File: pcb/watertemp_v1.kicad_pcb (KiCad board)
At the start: 2 copper layers, 43 x 90 mm, 31 parts, among them J1 RN2483 Ext, J2 SWD, J3 I2C, J4 UART1, J5 UART2, U1 LPC11U24FBD48, U2 RN2483, U3 SHT21, U4 LP5907-Q1, U5 DS18B20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

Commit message: Finish routing first version
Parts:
- added C6: 100nF, Capacitors_SMD:C_0805, F.Cu at (68.8, 53.8)
- added C7: 100nF, Capacitors_SMD:C_0805, F.Cu at (63.6, 65.8)
- added REF**: VIA-0.6mm, StitchingVia:VIA-0.6mm, F.Cu at (73.0, 63.9)
- added REF**: VIA-0.6mm, StitchingVia:VIA-0.6mm, F.Cu at (61.3, 106.7)
- added REF**: VIA-0.6mm, StitchingVia:VIA-0.6mm, F.Cu at (62.1, 105.9)
- added REF**: VIA-0.6mm, StitchingVia:VIA-0.6mm, F.Cu at (60.5, 104.4)
- added REF**: VIA-0.6mm, StitchingVia:VIA-0.6mm, F.Cu at (59.7, 105.2)
- added REF**: VIA-0.6mm, StitchingVia:VIA-0.6mm, F.Cu at (58.9, 105.9)
- added REF**: VIA-0.6mm, StitchingVia:VIA-0.6mm, F.Cu at (72.3, 51.7)
- added REF**: VIA-0.6mm, StitchingVia:VIA-0.6mm, F.Cu at (67.7, 63.9)
- added REF**: VIA-0.6mm, StitchingVia:VIA-0.6mm, F.Cu at (75.6, 56.5)
- added REF**: VIA-0.6mm, StitchingVia:VIA-0.6mm, F.Cu at (65.3, 102.5)
- added REF**: VIA-0.6mm, StitchingVia:VIA-0.6mm, F.Cu at (64.5, 103.3)
- added REF**: VIA-0.6mm, StitchingVia:VIA-0.6mm, F.Cu at (67.3, 103.6)
- added REF**: VIA-0.6mm, StitchingVia:VIA-0.6mm, F.Cu at (66.5, 104.4)
- added REF**: VIA-0.6mm, StitchingVia:VIA-0.6mm, F.Cu at (65.8, 105.2)
- added REF**: VIA-0.6mm, StitchingVia:VIA-0.6mm, F.Cu at (60.6, 107.4)
- R1, R2, R3, R4, R5, R6, R7: footprint Resistors_SMD:R_0805_HandSoldering -> Resistors_SMD:R_0805
- moved R7 94.6 mm to (30.4, 74.0)
- moved D3 92.1 mm to (32.0, 65.0)
- moved R2 84.1 mm to (36.3, 61.2), turned to 180 degrees
- moved R3 82.6 mm to (36.3, 65.0), turned to 180 degrees
- moved R6 82.1 mm to (30.4, 76.6)
- moved D1 80.4 mm to (32.0, 57.4)
- moved R8 77.8 mm to (30.5, 99.5), turned to 270 degrees
- moved U5 77.0 mm to (34.2, 103.4), turned to 180 degrees
- moved R1 73.8 mm to (36.3, 57.4), turned to 180 degrees
- moved D2 73.6 mm to (32.0, 61.2)
- moved J3 43.4 mm to (34.2, 71.5), turned to 0 degrees
- moved J1 40.0 mm to (75.9, 71.9)
- moved R4 38.2 mm to (63.6, 56.8), turned to 270 degrees
- moved R5 24.5 mm to (75.0, 68.8)
- moved J2 21.3 mm to (74.0, 47.0), turned to 0 degrees
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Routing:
- net 3.3V: track 3.92 -> 236.2 mm, vias 0 -> 2
- net SCL: track 0.00 -> 120.4 mm, vias 0 -> 2
- net SDA: track 0.00 -> 114.0 mm, vias 0 -> 2
- net UC-TX0: track 0.00 -> 83.3 mm, vias 0 -> 2
- net UC-RX0: track 0.00 -> 80.0 mm, vias 0 -> 2
- net DS18B20: track 0.00 -> 62.9 mm, vias 0 -> 2
- net LED1: track 0.00 -> 45.6 mm, vias 0 -> 2
- net LED2: track 0.00 -> 35.8 mm, vias 0 -> 2
- net LED3: track 0.00 -> 35.2 mm, vias 0 -> 2
- net UC-TX1: track 0.00 -> 32.2 mm, vias 0 -> 1
- net UC-RX1: track 0.00 -> 31.8 mm, vias 0 -> 1
- net PGD_INT: track 0.00 -> 30.2 mm, vias 0 -> 1
- net PGC_INT: track 0.00 -> 29.9 mm, vias 0 -> 1
- net RN_RST: track 0.00 -> 27.5 mm
- net NRESET: track 0.00 -> 21.6 mm, vias 0 -> 2
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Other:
- board size 43 x 90 mm -> 56 x 90 mm
- net class PWR: clearance 0.25 -> 0.2
- board text added: "3.3V"
- board text added: "Data"
- board text added: "GND"
- board text added: "SCL"
- board text added: "SDA"

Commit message: Some more details
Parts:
- AE1: value Antenna_Shield -> SMA
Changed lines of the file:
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@@
     (links 111)
     (no_connects 0)
-    (area 25.4 37.719 91.100001 131.826001)
+    (area 26.924999 39.924999 83.075001 130.075001)
     (thickness 1.6)
     (drawings 26)
@@
       (net 1 GND))
     (model ${KISYS3DMOD}/Pin_Headers.3dshapes/Pin_Header_Straight_1x07_Pitch2.54mm.wrl
-      (at (xyz 0 0 0))
-      (scale (xyz 1 1 1))
-      (rotate (xyz 0 0 0))
+      (at (xyz 0 -0.3 0))
+      (scale (xyz 1 1 1))
+      (rotate (xyz 0 0 90))
     )
   )
@@
     (pad 1 np_thru_hole circle (at 0 0) (size 3.5 3.5) (drill 3.5) (layers *.Cu *.Mask))
   )
-  (module RF:SMA_EDGE (layer F.Cu)
-    (at 66.05 113.0375 270)
-    (tags "SMA Edge Mount RF Antenna Connector")
-    (fp_text reference AE1 (at -6.35 2.54 360) (layer F.SilkS) hide
-      (effects (font (size 1 1) (thickness 0.15)))
-    )
-    (fp_text value Antenna_Shield (at 0 6.35 270) (layer F.Fab) hide
-      (effects (font (size 1 1) (thickness 0.15)))
-    )
-    (fp_line (start -4.7625 -1.651) (end 4.7625 -1.651) (layer F.SilkS) (width 0.2))
-    (fp_line (start -4.7625 -1.651) (end -4.7625 4.7498) (layer F.SilkS) (width 0.2))
-    (fp_line (start -2.38 -1.651) (end -2.38 -9.525) (layer F.SilkS) (width 0.2))
-    (fp_line (start -4.7625 4.7498) (end 4.7625 4.7498) (layer F.SilkS) (width 0.2))
-    (fp_line (start -4.7625 0) (end 4.7625 0) (layer F.SilkS) (width 0.2))
-    (fp_line (start 4.7625 -1.651) (end 4.7625 4.7498) (layer F.SilkS) (width 0.2))
-    (fp_line (start 2.38 -1.651) (end 2.38 -9.525) (layer F.SilkS) (width 0.2))
-    (fp_line (start -2.38 -9.525) (end 2.38 -9.525) (layer F.SilkS) (width 0.2))
-    (pad 2 smd rect (at -3.9625 2.55 270) (size 1.6 5.1) (layers F.Cu F.Paste F.Mask)
-      (net 1 GND))
-    (pad 1 smd rect (at 0 2.55 270) (size 1.1 5.1) (layers F.Cu F.Paste F.Mask)
-      (net 2 "Net-(AE1-Pad1)"))
-    (pad 2 smd rect (at 3.9625 2.55 270) (size 1.6 5.1) (layers F.Cu F.Paste F.Mask)
-      (net 1 GND))
-    (pad 2 smd rect (at -3.9625 2.55 270) (size 1.6 5.1) (layers B.Cu F.Paste F.Mask)
-      (net 1 GND))
-    (pad 2 smd rect (at 3.9625 2.55 270) (size 1.6 5.1) (layers B.Cu F.Paste F.Mask)
-      (net 1 GND))
-  )
   (module Capacitors_SMD:C_0805 (layer F.Cu)
     (at 61.087 65.786 270)
@@
       (net 1 GND))
     (model ${KISYS3DMOD}/Pin_Headers.3dshapes/Pin_Header_Straight_1x04_Pitch2.54mm.wrl
-      (at (xyz 0 0 0))
-      (scale (xyz 1 1 1))
-      (rotate (xyz 0 0 0))
+      (at (xyz 0 -0.15 0))
+      (scale (xyz 1 1 1))
+      (rotate (xyz 0 0 90))
     )
   )
@@
       (net 21 UC-TX1))
     (model ${KISYS3DMOD}/Pin_Headers.3dshapes/Pin_Header_Straight_1x02_Pitch2.54mm.wrl
-      (at (xyz 0 0 0))
-      (scale (xyz 1 1 1))
-      (rotate (xyz 0 0 0))
+      (at (xyz 0 -0.05 0))
+      (scale (xyz 1 1 1))
+      (rotate (xyz 0 0 90))
     )
   )
@@
     (pad 2 smd rect (at 0 0) (size 2.4 1.5) (layers F.Cu F.Paste F.Mask)
       (net 1 GND))
+    (model Housings_DFN_QFN.3dshapes/DFN-6-1EP_3x3mm_Pitch0.95mm.wrl
+      (at (xyz 0 0 0))
+      (scale (xyz 1 1 1))
+      (rotate (xyz 0 0 0))
+    )
   )
   (module TO_SOT_Packages_SMD:SOT-23-6 (layer F.Cu)
@@
       (net 6 3.3V))
     (model ${KISYS3DMOD}/Pin_Headers.3dshapes/Pin_Header_Straight_1x03_Pitch2.54mm.wrl
-      (at (xyz 0 0 0))
-      (scale (xyz 1 1 1))
-      (rotate (xyz 0 0 0))
+      (at (xyz 0 -0.1 0))
+      (scale (xyz 1 1 1))
+      (rotate (xyz 0 0 90))
     )
   )
@@
       (net 8 UC-TX0))
     (model ${KISYS3DMOD}/Pin_Headers.3dshapes/Pin_Header_Straight_1x02_Pitch2.54mm.wrl
-      (at (xyz 0 0 0))
-      (scale (xyz 1 1 1))
-      (rotate (xyz 0 0 0))
+      (at (xyz 0 -0.05 0))
+      (scale (xyz 1 1 1))
+      (rotate (xyz 0 0 90))
     )
   )
@@
     (pad 3 smd rect (at 1.1 -0.85 270) (size 1.4 1.2) (layers F.Cu F.Paste F.Mask))
     (pad 4 smd rect (at -1.1 -0.85 270) (size 1.4 1.2) (layers F.Cu F.Paste F.Mask))
-    (model ${KISYS3DMOD}/Crystals.3dshapes/Crystal_SMD_Abracon_ABM8G-4pin_3.2x2.5mm.wrl
-      (at (xyz 0 0 0))
-      (scale (xyz 1 1 1))
+    (model ${KISYS3DMOD}/Crystals.3dshapes/Crystal_SMD_SeikoEpson_TSX3225-4pin_3.2x2.5mm.wrl
+      (at (xyz 0 0 0))
+      (scale (xyz 0.25 0.25 0.25))
       (rotate (xyz 0 0 0))
     )
@@
       (rotate (xyz 0 0 0))
     )
+  )
+  (module RF:SMA_EDGE (layer F.Cu)
+    (at 66.05 113.0375 270)
+    (tags "SMA Edge Mount RF Antenna Connector")
+    (fp_text reference AE1 (at -6.35 2.54 360) (layer F.Fab)
+      (effects (font (size 1 1) (thickness 0.15)))
+    )
+    (fp_text value SMA (at 3.53834 6.38032 270) (layer F.Fab)
+      (effects (font (size 1 1) (thickness 0.15)))
+    )
+    (fp_line (start -4.7625 -1.651) (end 4.7625 -1.651) (layer F.Fab) (width 0.2))
+    (fp_line (start -4.7625 -1.651) (end -4.7625 4.7498) (layer F.Fab) (width 0.2))
+    (fp_line (start -2.38 -1.651) (end -2.38 -9.525) (layer F.Fab) (width 0.2))
+    (fp_line (start -4.7625 4.7498) (end 4.7625 4.7498) (layer F.Fab) (width 0.2))
+    (fp_line (start -4.7625 0) (end 4.7625 0) (layer F.Fab) (width 0.2))
+    (fp_line (start 4.7625 -1.651) (end 4.7625 4.7498) (layer F.Fab) (width 0.2))
+    (fp_line (start 2.38 -1.651) (end 2.38 -9.525) (layer F.Fab) (width 0.2))
+    (fp_line (start -2.38 -9.525) (end 2.38 -9.525) (layer F.Fab) (width 0.2))
+    (pad 2 smd rect (at -3.9625 2.55 270) (size 1.6 5.1) (layers F.Cu F.Paste F.Mask)
+      (net 1 GND))
+    (pad 1 smd rect (at 0 2.55 270) (size 1.1 5.1) (layers F.Cu F.Paste F.Mask)
+      (net 2 "Net-(AE1-Pad1)"))
+    (pad 2 smd rect (at 3.9625 2.55 270) (size 1.6 5.1) (layers F.Cu F.Paste F.Mask)
+      (net 1 GND))
+    (pad 2 smd rect (at -3.9625 2.55 270) (size 1.6 5.1) (layers B.Cu F.Paste F.Mask)
+      (net 1 GND))
+    (pad 2 smd rect (at 3.9625 2.55 270) (size 1.6 5.1) (layers B.Cu F.Paste F.Mask)
+      (net 1 GND))
   )
   (gr_text GND (at 36.195 103.378) (layer F.SilkS)
@@
   (segment (start 79.052499 128.134001) (end 80.2025 126.984) (width 0.4) (layer F.Cu) (net 1))
   (segment (start 80.2025 126.984) (end 80.3275 126.984) (width 0.4) (layer F.Cu) (net 1))
+  (segment (start 63.5 113.0375) (end 60.75922 113.0375) (width 1.016) (layer F.Cu) (net 2))
+  (segment (start 60.75922 113.0375) (end 59.309 111.58728) (width 1.016) (layer F.Cu) (net 2))
+  (segment (start 59.309 111.58728) (end 59.309 107.1118) (width 1.016) (layer F.Cu) (net 2))
+  (segment (start 59.309 107.1118) (end 61.849 104.5718) (width 1.016) (layer F.Cu) (net 2))
   (segment (start 61.849 104.5718) (end 64.8462 104.5718) (width 1.016) (layer F.Cu) (net 2))
-  (segment (start 63.5 113.0375) (end 61.5 113.0375) (width 1.016) (layer F.Cu) (net 2))
-  (segment (start 61.5 113.0375) (end 59.309 110.8465) (width 1.016) (layer F.Cu) (net 2))
-  (segment (start 59.309 110.8465) (end 59.309 107.1118) (width 1.016) (layer F.Cu) (net 2))
-  (segment (start 59.309 107.1118) (end 61.849 104.5718) (width 1.016) (layer F.Cu) (net 2))
   (segment (start 64.8462 104.5718) (end 66.548 102.87) (width 1.016) (layer F.Cu) (net 2))
   (segment (start 66.548 102.87) (end 66.548 100.7872) (width 1.016) (layer F.Cu) (net 2))

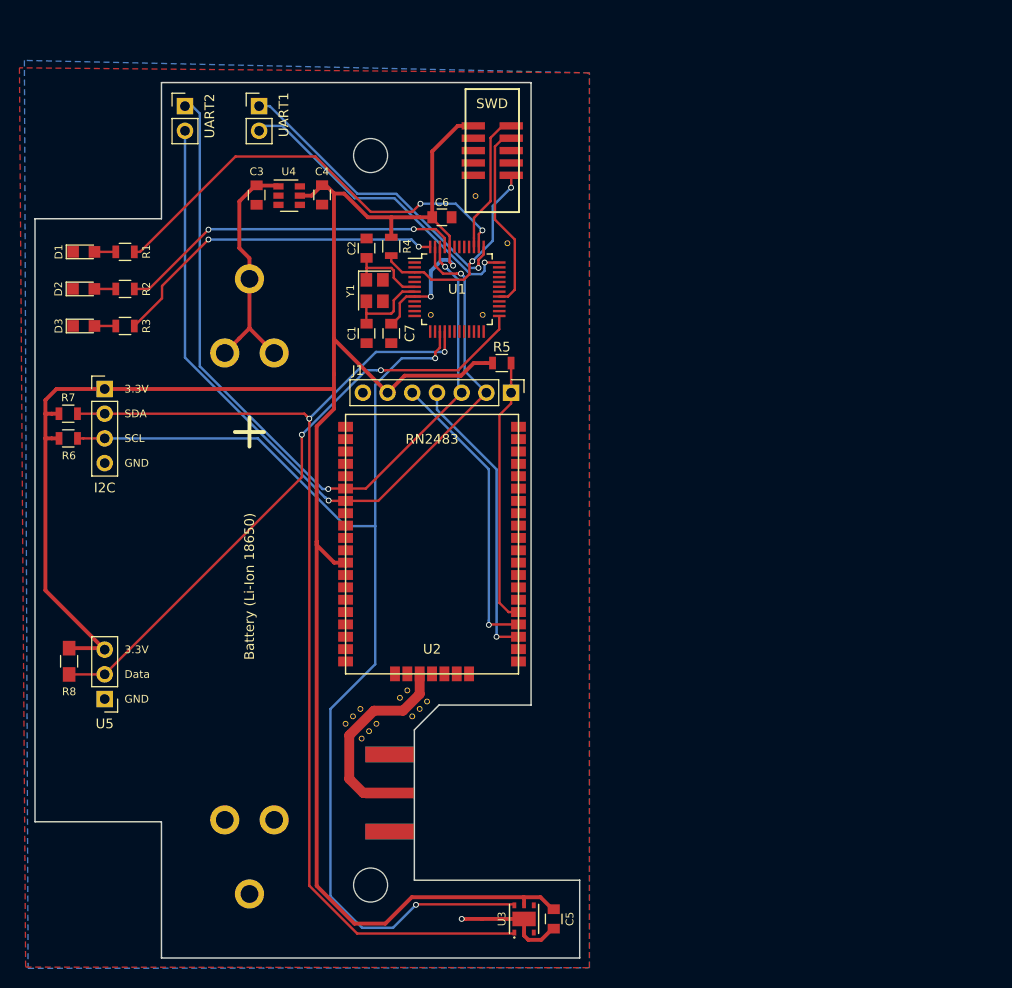
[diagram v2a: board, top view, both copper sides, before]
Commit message: Enlarge some of the pads for hand soldering
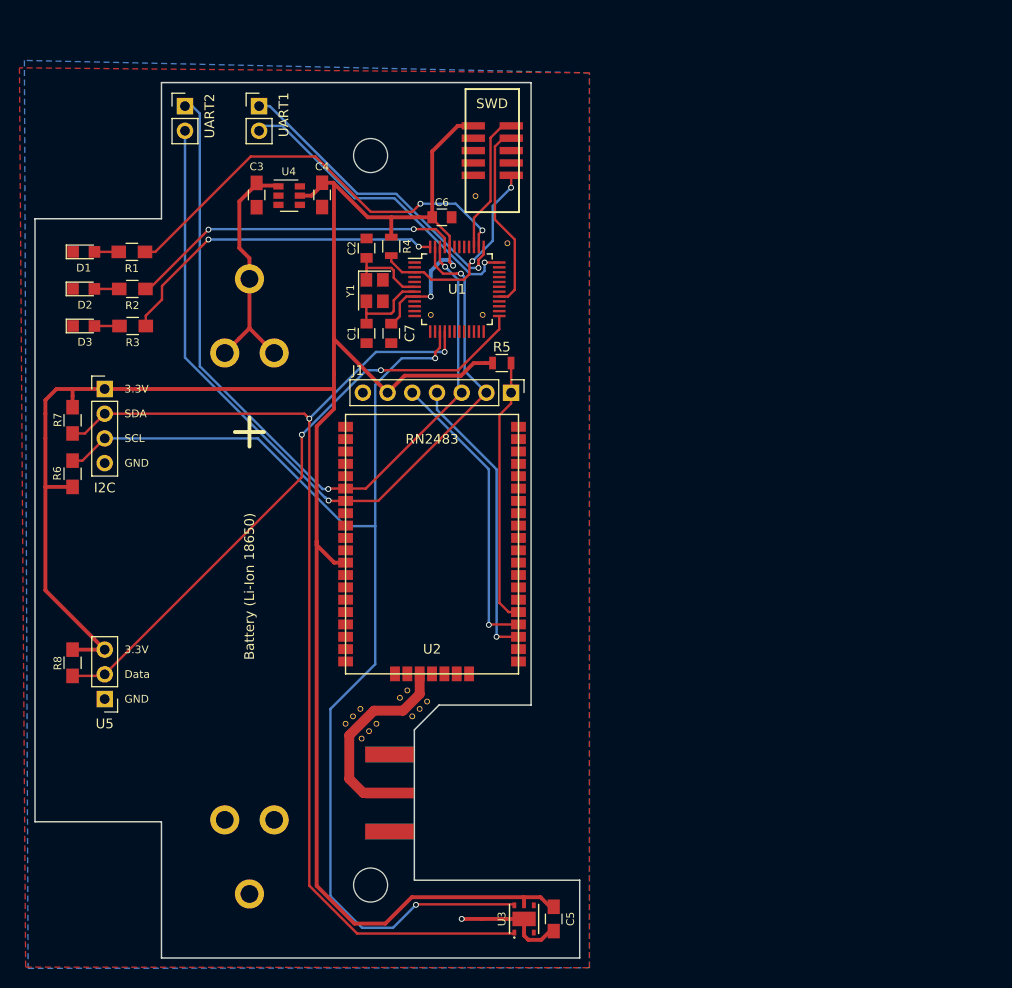
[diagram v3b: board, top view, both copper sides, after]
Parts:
- C3, C4, C5: footprint Capacitors_SMD:C_0805 -> Capacitors_SMD:C_0805_HandSoldering
- R1, R2, R3, R6, R7: footprint Resistors_SMD:R_0805 -> Resistors_SMD:R_0805_HandSoldering
- moved R6 3.66 mm to (30.9, 80.2), turned to 90 degrees
- moved R7 0.82 mm to (30.9, 74.7), turned to 270 degrees
- moved R3 0.78 mm to (37.0, 65.0)
- moved R2 0.75 mm to (37.0, 61.2)
- moved R1 0.70 mm to (37.0, 57.4)
- moved R8 0.39 mm to (30.9, 99.6)
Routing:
- net 3.3V: track 236.2 -> 239.0 mm
- net SCL: track 120.4 -> 121.8 mm
- net SDA: track 114.0 -> 115.4 mm
- net LED2: track 35.8 -> 34.6 mm
- net LED1: track 45.6 -> 44.4 mm

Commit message: Add OSHW and Coredump logos (fixes #5)
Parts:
- added G***: LOGO, Logos:Coredump-Logo_32.2x13.3mm_Silkscreen, B.Cu at (44.5, 95.5)
- added REF***: OSHW-Logo_5.7x6mm_Copper, Logos:OSHW-Logo_5.7x6mm_Mask, F.Cu at (33.7, 88.5)
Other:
- board text added: "coredump.ch v1.0 2017"
- board text added: "https://github.com/coredump-ch/watertemp-hardware"
